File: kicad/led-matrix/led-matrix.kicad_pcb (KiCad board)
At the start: 2 copper layers, 59.7 x 59.7 mm, 18 parts, among them J1 INPUT_CONN, J2 OUTPUT_CONN, U1 74HCT4051, U2 MIC2981_82YN, U3 TPIC6C595N

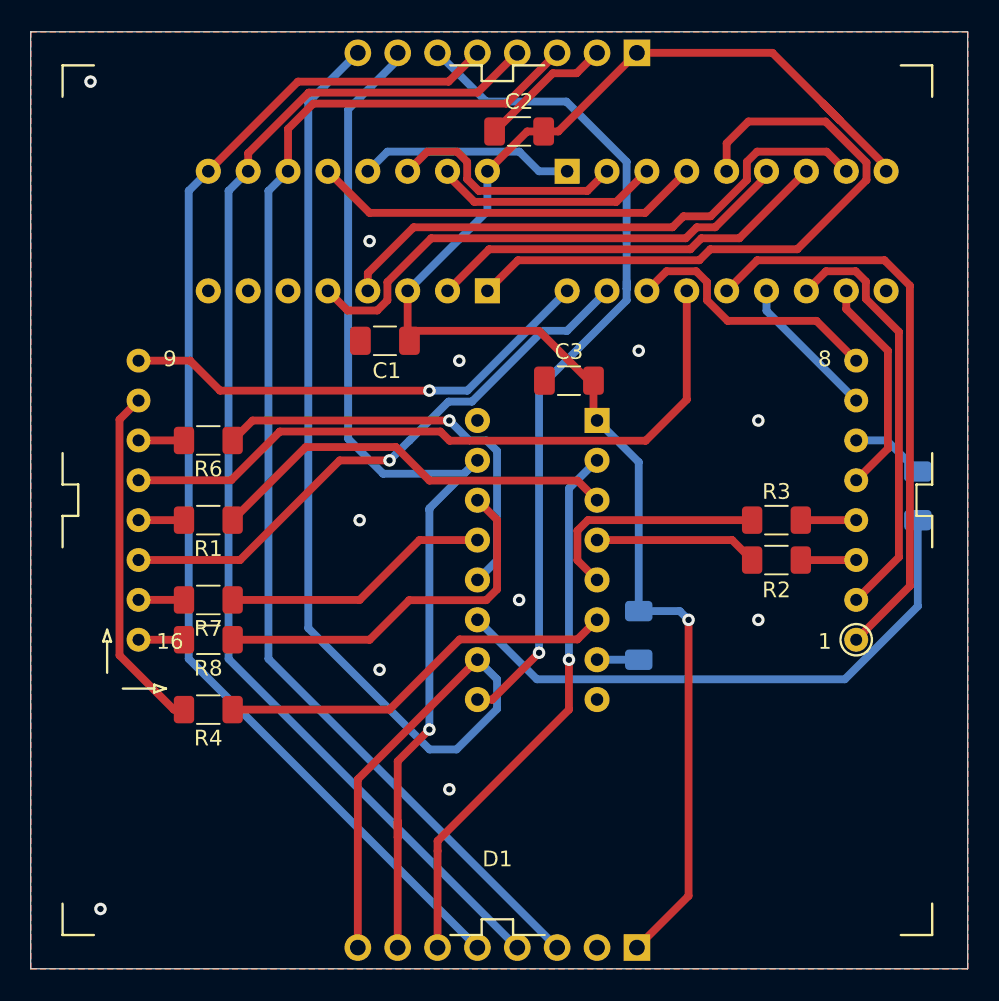
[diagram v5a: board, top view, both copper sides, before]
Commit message: Tweak silk screen
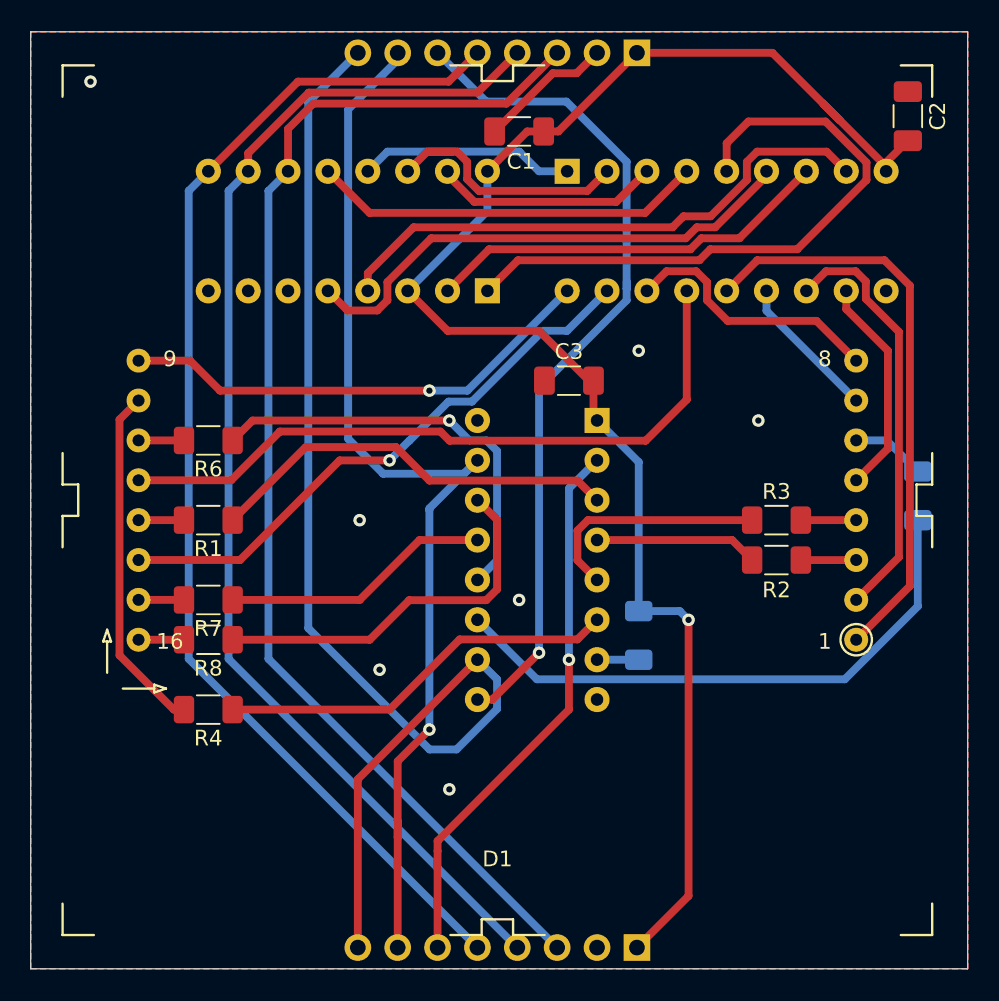
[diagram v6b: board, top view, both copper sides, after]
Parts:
- added ?: , , F.Cu at (46.7, 28.7)
- added ?: , , F.Cu at (47.0, 79.2)
- added ?: , , F.Cu at (-1.91, 16.5)
- added ?: , , F.Cu at (55.9, 22.2)
- added ?: , , F.Cu at (-17.8, 14.0)
- added ?: , , F.Cu at (5.71, 14.0)
- moved C2 24.8 mm to (74.3, 28.9), turned to 90 degrees
- moved C1 15.8 mm to (49.5, 29.8)
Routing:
- net /VCC: track 100.5 -> 101.6 mm
- net /GND: vias 11 -> 7
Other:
- board text added: "GND"
- board text added: "VCC"
- board text added: "r_clk"
- board text added: "s0"
- board text added: "s1"
- board text added: "s2"
- board text added: "serial_clk"
- board text added: "serial_in"
- board text added: "serial_out"
